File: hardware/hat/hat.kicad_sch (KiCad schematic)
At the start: 6 parts, among them J1 GPIO, U1 CAT24C256

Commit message: hw: really close!!
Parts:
- added C13, C14: 1uF, symbol Device:C_Small
- added J6: Uart, symbol Connector:Conn_01x03_Pin
- added R3: 10k, symbol Device:R_Small
- added U3: TPS7A20xxxDBV, Package_TO_SOT_SMD:SOT-23-5, symbol Regulator_Linear:TPS7A20xxxDBV
- added U4: Oled, symbol util:oled
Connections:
- net +3V3: now also C13.1, U3.1 (IN), U4.1 (VCC)
- net GND: now also C13.2, C14.2, J6.1 (Pin_1), R3.2, U3.2 (GND), U4.2 (GND)
- net GPIO10/SPI0.MOSI: now also U4.3 (DIN)
- net GPIO11/SPI0.SCLK: now also U4.4 (CLK)
- net GPIO14/TXD0: now also J6.2 (Pin_2)
- net GPIO15/RXD0: now also J6.3 (Pin_3)
- net GPIO25: now also U4.6 (DC)
- net GPIO27: now also U4.7 (RST)
- net GPIO8/SPI0.CE0: now also U4.5 (CS)
- net GPIO23 renamed 1V8_EN
- net 1V8_EN: now also R3.1, U3.3 (EN)
- new net +1V8: C14.1, U3.5 (OUT)
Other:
- note added: "note: CM4 DIN = Codec DOUT"

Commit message: hw: assign
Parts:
- added TP17: LDO_IN, TestPoint:TestPoint_Pad_D2.0mm, symbol Connector:TestPoint
- added TP18: LDO_OUT, TestPoint:TestPoint_Pad_D2.0mm, symbol Connector:TestPoint
- added TP19: 5V, TestPoint:TestPoint_THTPad_1.5x1.5mm_Drill0.7mm, symbol Connector:TestPoint
- added TP20: GND, TestPoint:TestPoint_THTPad_1.5x1.5mm_Drill0.7mm, symbol Connector:TestPoint
- added TP21: 3V3, TestPoint:TestPoint_THTPad_1.5x1.5mm_Drill0.7mm, symbol Connector:TestPoint
- C1: footprint (none) -> Capacitor_SMD:C_0805_2012Metric
- C2: renamed from C13; footprint (none) -> Capacitor_SMD:C_0805_2012Metric
- C3: renamed from C14; footprint (none) -> Capacitor_SMD:C_0805_2012Metric
- J2: renamed from J6; footprint (none) -> Connector_PinHeader_2.54mm:PinHeader_1x03_P2.54mm_Vertical
- JP1: footprint (none) -> Jumper:SolderJumper-3_P1.3mm_Open_RoundedPad1.0x1.5mm_NumberLabels
- R1: renamed from R3; footprint (none) -> Resistor_SMD:R_0805_2012Metric
- R2: renamed from R1; footprint (none) -> Resistor_SMD:R_0805_2012Metric
- R3: renamed from R2; footprint (none) -> Resistor_SMD:R_0805_2012Metric
- U1: footprint (none) -> Package_SO:SOIC-8_3.9x4.9mm_P1.27mm
- U3: renamed from U4; footprint (none) -> Connector_PinHeader_2.54mm:PinHeader_1x07_P2.54mm_Vertical
- renumbered U3 to U2
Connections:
- net +1V8: now also TP18.1
- net +3V3: now also TP17.1, TP21.1
- net +5V: now also TP19.1
- net GND: now also TP20.1

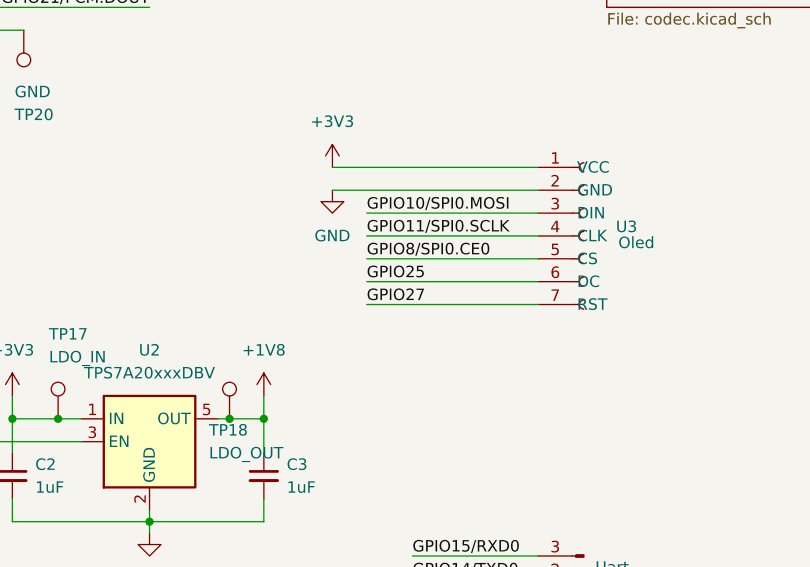
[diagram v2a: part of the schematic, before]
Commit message: all signal except ID chip
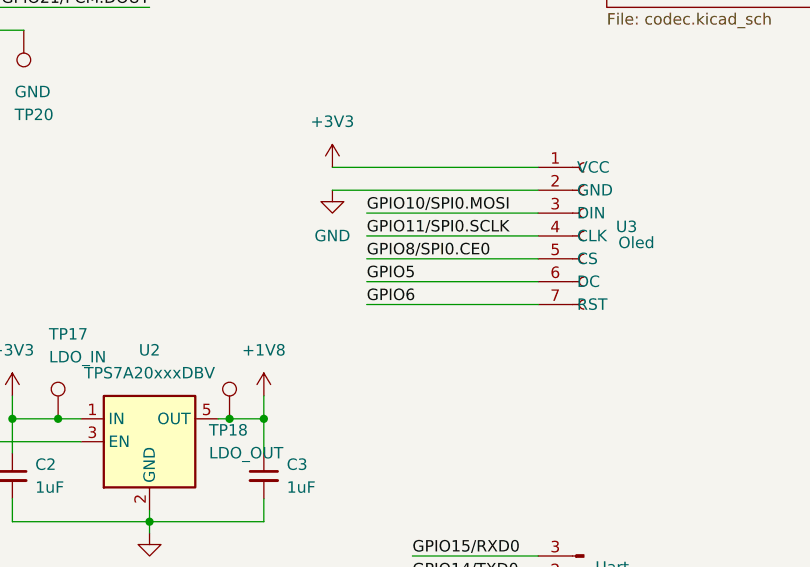
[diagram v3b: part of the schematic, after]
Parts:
- JP1: footprint Jumper:SolderJumper-3_P1.3mm_Open_RoundedPad1.0x1.5mm_NumberLabels -> Jumper:SolderJumper-2_P1.3mm_Open_RoundedPad1.0x1.5mm
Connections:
- net GPIO25: no longer U3.6 (DC)
- net GPIO27: no longer U3.7 (RST)
- net GPIO5: now also U3.6 (DC)
- net GPIO6: now also U3.7 (RST)
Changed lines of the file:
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@@
 		)
 	)
-	(label "GPIO27"
+	(label "GPIO6"
 		(at 124.46 109.22 0)
 		(effects
@@
 		)
 	)
-	(label "GPIO25"
+	(label "GPIO5"
 		(at 124.46 106.68 0)
 		(effects
@@
 			)
 		)
-		(property "Footprint" "Jumper:SolderJumper-3_P1.3mm_Open_RoundedPad1.0x1.5mm_NumberLabels"
+		(property "Footprint" "Jumper:SolderJumper-2_P1.3mm_Open_RoundedPad1.0x1.5mm"
 			(at 96.52 180.34 0)
 			(hide yes)

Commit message: all signals
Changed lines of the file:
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@@
 		)
 	)
-	(label "GPIO22"
+	(label "GPIO24"
 		(at 132.08 46.99 0)
 		(effects

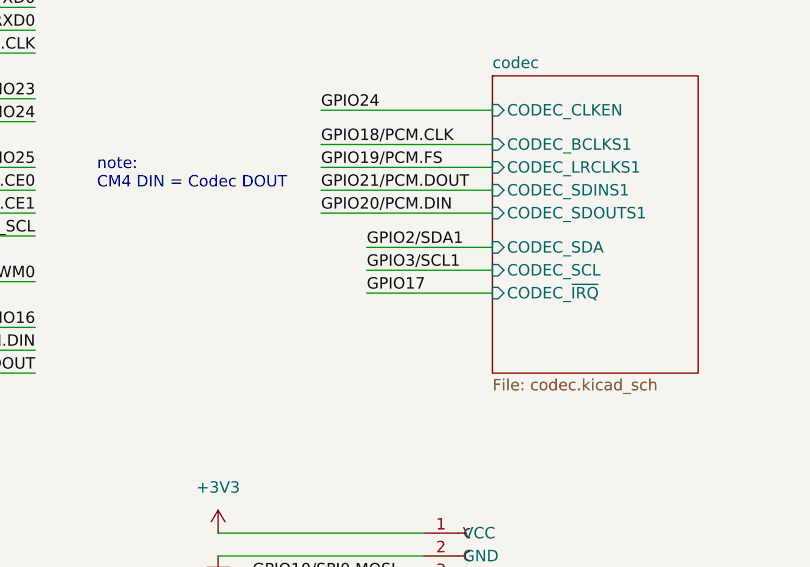
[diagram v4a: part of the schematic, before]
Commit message: vias for planes
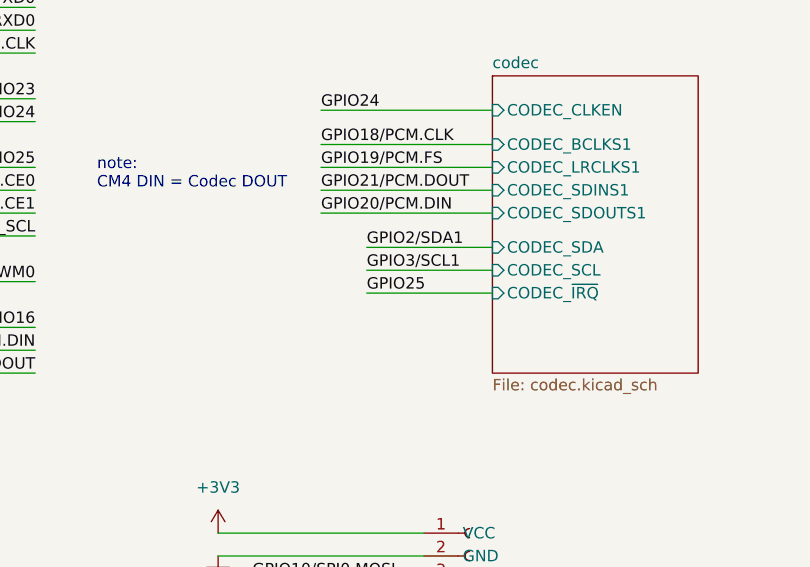
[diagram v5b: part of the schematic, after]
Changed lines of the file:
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@@
 		)
 	)
-	(label "GPIO17"
+	(label "GPIO25"
 		(at 137.16 67.31 0)
 		(effects

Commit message: before drc
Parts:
- removed TP21: 3V3, TestPoint:TestPoint_THTPad_1.5x1.5mm_Drill0.7mm, symbol Connector:TestPoint
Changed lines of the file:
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@@
-	(wire
-		(pts
-			(xy 48.26 27.94) (xy 55.88 27.94)
-		)
-		(stroke
-			(width 0)
-			(type default)
-		)
-	)
 	(wire
 		(pts
@@
 					(unit 1)
 				)
-			)
-		)
-	)
-	(symbol
-		(lib_id "Connector:TestPoint")
-		(at 48.26 27.94 0)
-		(unit 1)
-		(body_style 1)
-		(exclude_from_sim no)
-		(in_bom yes)
-		(on_board yes)
-		(in_pos_files yes)
-		(dnp no)
-		(property "Reference" "TP21"
-			(at 47.244 18.542 0)
-			(show_name no)
-			(do_not_autoplace no)
-			(effects
-				(font
-					(size 1.27 1.27)
-				)
-				(justify left)
-			)
-		)
-		(property "Value" "3V3"
-			(at 47.244 21.082 0)
-			(show_name no)
-			(do_not_autoplace no)
-			(effects
-				(font
-					(size 1.27 1.27)
-				)
-				(justify left)
-			)
-		)
-		(property "Footprint" "TestPoint:TestPoint_THTPad_1.5x1.5mm_Drill0.7mm"
-			(at 53.34 27.94 0)
-			(hide yes)
-			(show_name no)
-			(do_not_autoplace no)
-			(effects
-				(font
-					(size 1.27 1.27)
-				)
-			)
-		)
-		(property "Datasheet" ""
-			(at 53.34 27.94 0)
-			(hide yes)
-			(show_name no)
-			(do_not_autoplace no)
-			(effects
-				(font
-					(size 1.27 1.27)
-				)
-			)
-		)
-		(property "Description" "test point"
-			(at 48.26 27.94 0)
-			(hide yes)
-			(show_name no)
-			(do_not_autoplace no)
-			(effects
-				(font
-					(size 1.27 1.27)
-				)
-			)
-		)
-		(pin "1"
-		)
-		(instances
-			(project "hat"
-				(path "/e63e39d7-6ac0-4ffd-8aa3-1841a4541b55"
-					(reference "TP21")
-					(unit 1)
-				)

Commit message: wip
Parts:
- TP17, TP18, TP19, TP20: now not fitted
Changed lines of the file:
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@@
 		(on_board yes)
 		(in_pos_files yes)
-		(dnp no)
+		(dnp yes)
 		(property "Reference" "TP20"
 			(at 85.344 88.138 0)
@@
 		(on_board yes)
 		(in_pos_files yes)
-		(dnp no)
+		(dnp yes)
 		(property "Reference" "TP19"
 			(at 81.534 18.542 0)
@@
 		(on_board yes)
 		(in_pos_files yes)
-		(dnp no)
+		(dnp yes)
 		(property "Reference" "TP17"
 			(at 89.154 112.522 0)
@@
 		(on_board yes)
 		(in_pos_files yes)
-		(dnp no)
+		(dnp yes)
 		(property "Reference" "TP18"
 			(at 106.934 123.19 0)

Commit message: restore backup from June 6 1:34 AM
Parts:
- C1: value 100n -> 100nF; LCSC (none) -> C49678
- C2, C3: LCSC (none) -> C28323
- J1: LCSC (none) -> C2977589
- J2, JP1, U3: now not fitted
- R1: LCSC (none) -> C17414
- R2, R3: LCSC (none) -> C17614
- U1: LCSC (none) -> C79987
- U2: LCSC (none) -> C2862740
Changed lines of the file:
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@@
+			)
+		)
+		(property "LCSC" "C2977589"
+			(at 66.04 50.8 0)
+			(hide yes)
+			(show_name no)
+			(do_not_autoplace no)
+			(effects
+				(font
+					(size 1.27 1.27)
+				)
 			)
 		)
@@
 			)
 		)
-		(property "Value" "100n"
+		(property "Value" "100nF"
 			(at 64.9858 178.9493 0)
 			(show_name no)
@@
 		)
 		(property "Description" "Unpolarized capacitor, small symbol"
+			(at 67.31 177.8 0)
+			(hide yes)
+			(show_name no)
+			(do_not_autoplace no)
+			(effects
+				(font
+					(size 1.27 1.27)
+				)
+			)
+		)
+		(property "LCSC" "C49678"
 			(at 67.31 177.8 0)
 			(hide yes)
@@
 		)
 		(property "Description" "Resistor, small symbol"
+			(at 93.98 170.18 0)
+			(hide yes)
+			(show_name no)
+			(do_not_autoplace no)
+			(effects
+				(font
+					(size 1.27 1.27)
+				)
+			)
+		)
+		(property "LCSC" "C17614"
 			(at 93.98 170.18 0)
 			(hide yes)
@@
 			)
 		)
+		(property "LCSC" "C2862740"
+			(at 100.33 124.46 0)
+			(hide yes)
+			(show_name no)
+			(do_not_autoplace no)
+			(effects
+				(font
+					(size 1.27 1.27)
+				)
+			)
+		)
 		(pin "4"
 		)
@@
 			)
 		)
+		(property "LCSC" ""
+			(at 86.36 78.74 0)
+			(hide yes)
+			(show_name no)
+			(do_not_autoplace no)
+			(effects
+				(font
+					(size 1.27 1.27)
+				)
+			)
+		)
 		(pin "1"
 		)
@@
 		(on_board yes)
 		(in_pos_files yes)
-		(dnp no)
+		(dnp yes)
 		(property "Reference" "J2"
 			(at 149.86 140.9701 0)
@@
 			)
 		)
+		(property "LCSC" ""
+			(at 148.59 139.7 0)
+			(hide yes)
+			(show_name no)
+			(do_not_autoplace no)
+			(effects
+				(font
+					(size 1.27 1.27)
+				)
+			)
+		)
 		(pin "1"
 		)
@@
 		(on_board yes)
 		(in_pos_files yes)
-		(dnp no)
+		(dnp yes)
 		(property "Reference" "JP1"
 			(at 96.52 183.623 0)
@@
 		)
 		(property "Description" "Solder Jumper, 2-pole, open"
+			(at 96.52 180.34 0)
+			(hide yes)
+			(show_name no)
+			(do_not_autoplace no)
+			(effects
+				(font
+					(size 1.27 1.27)
+				)
+			)
+		)
+		(property "LCSC" ""
 			(at 96.52 180.34 0)
 			(hide yes)
@@
 			)
 		)
+		(property "LCSC" "C17614"
+			(at 101.6 170.18 0)
+			(hide yes)
+			(show_name no)
+			(do_not_autoplace no)
+			(effects
+				(font
+					(size 1.27 1.27)
+				)
+			)
+		)
 		(pin "1"
 		)
@@
 		(on_board yes)
 		(in_pos_files yes)
-		(dnp no)
+		(dnp yes)
 		(property "Reference" "U3"
 			(at 152.146 100.584 0)
@@
 		)
 		(property "Description" ""
+			(at 144.78 101.6 0)
+			(hide yes)
+			(show_name no)
+			(do_not_autoplace no)
+			(effects
+				(font
+					(size 1.27 1.27)
+				)
+			)
+		)
+		(property "LCSC" ""
 			(at 144.78 101.6 0)
 			(hide yes)
@@
 			)
 		)
+		(property "LCSC" "C28323"
+			(at 113.03 128.27 0)
+			(hide yes)
+			(show_name no)
+			(do_not_autoplace no)
+			(effects
+				(font
+					(size 1.27 1.27)
+				)
+			)
+		)
 		(pin "1"
 		)
@@
 		)
 		(property "Description" "256 kb CMOS Serial EEPROM, DIP-8/SOIC-8/TSSOP-8/DFN-8"
+			(at 81.28 177.8 0)
+			(hide yes)
+			(show_name no)
+			(do_not_autoplace no)
+			(effects
+				(font
+					(size 1.27 1.27)
+				)
+			)
+		)
+		(property "LCSC" "C79987"
 			(at 81.28 177.8 0)
 			(hide yes)
@@
 			)
 		)
+		(property "LCSC" ""
+			(at 82.55 27.94 0)
+			(hide yes)
+			(show_name no)
+			(do_not_autoplace no)
+			(effects
+				(font
+					(size 1.27 1.27)
+				)
+			)
+		)
 		(pin "1"
 		)
@@
 			)
 		)
+		(property "LCSC" ""
+			(at 90.17 121.92 0)
+			(hide yes)
+			(show_name no)
+			(do_not_autoplace no)
+			(effects
+				(font
+					(size 1.27 1.27)
+				)
+			)
+		)
 		(pin "1"
 		)
@@
 			)
 		)
+		(property "LCSC" "C17414"
+			(at 80.01 130.81 0)
+			(hide yes)
+			(show_name no)
+			(do_not_autoplace no)
+			(effects
+				(font
+					(size 1.27 1.27)
+				)
+			)
+		)
 		(pin "1"
 		)
@@
 		)
 		(property "Description" "test point"
+			(at 109.22 121.92 0)
+			(hide yes)
+			(show_name no)
+			(do_not_autoplace no)
+			(effects
+				(font
+					(size 1.27 1.27)
+				)
+			)
+		)
+		(property "LCSC" ""
 			(at 109.22 121.92 0)
 			(hide yes)
@@
 			(at 85.09 128.27 0)
 			(hide yes)
+			(show_name no)
+			(do_not_autoplace no)
+			(effects
+				(font
+					(size 1.27 1.27)
+				)
+			)
+		)
+		(property "LCSC" "C28323"
+			(at 85.09 128.27 0)
+			(hide yes)
